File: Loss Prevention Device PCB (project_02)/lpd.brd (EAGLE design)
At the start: 48.3 x 58.4 mm, 4 parts, among them U2 GT-U7, U3 HM-10

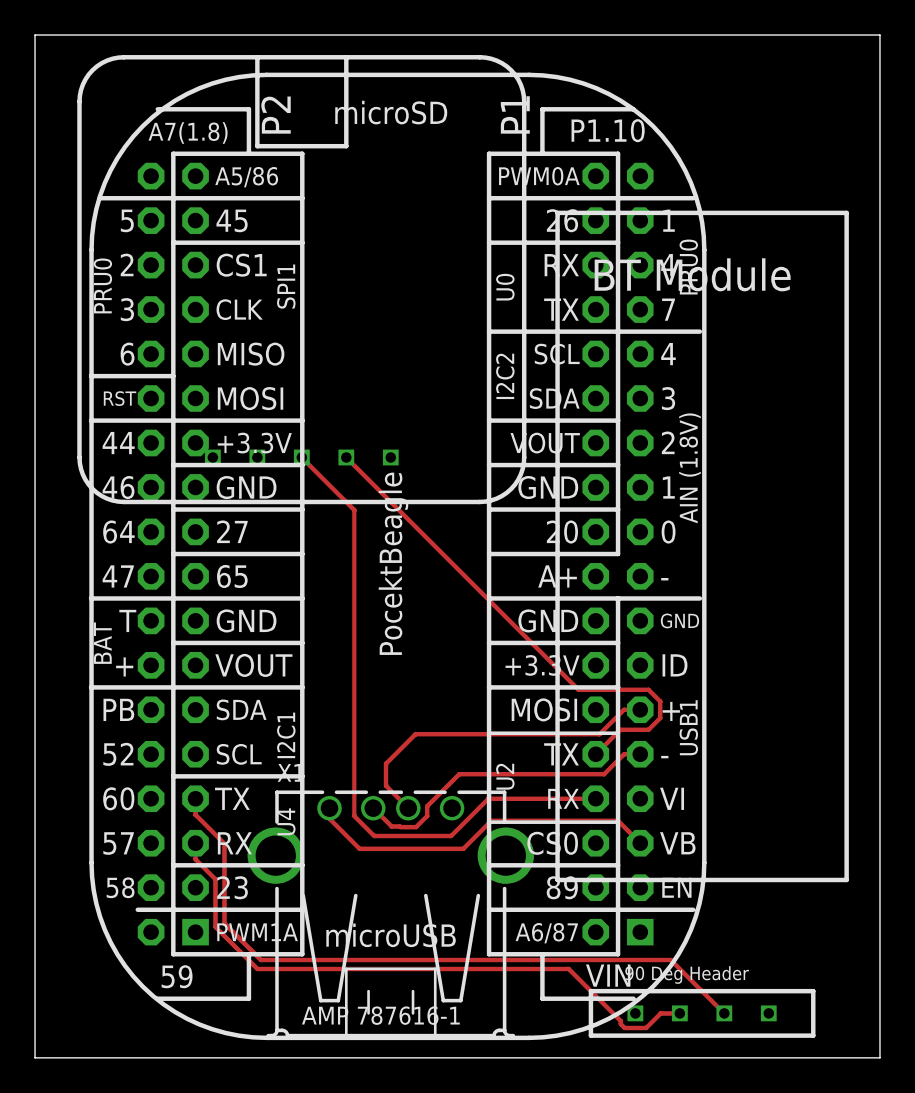
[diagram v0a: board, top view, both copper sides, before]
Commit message: Silkscreen cleanup
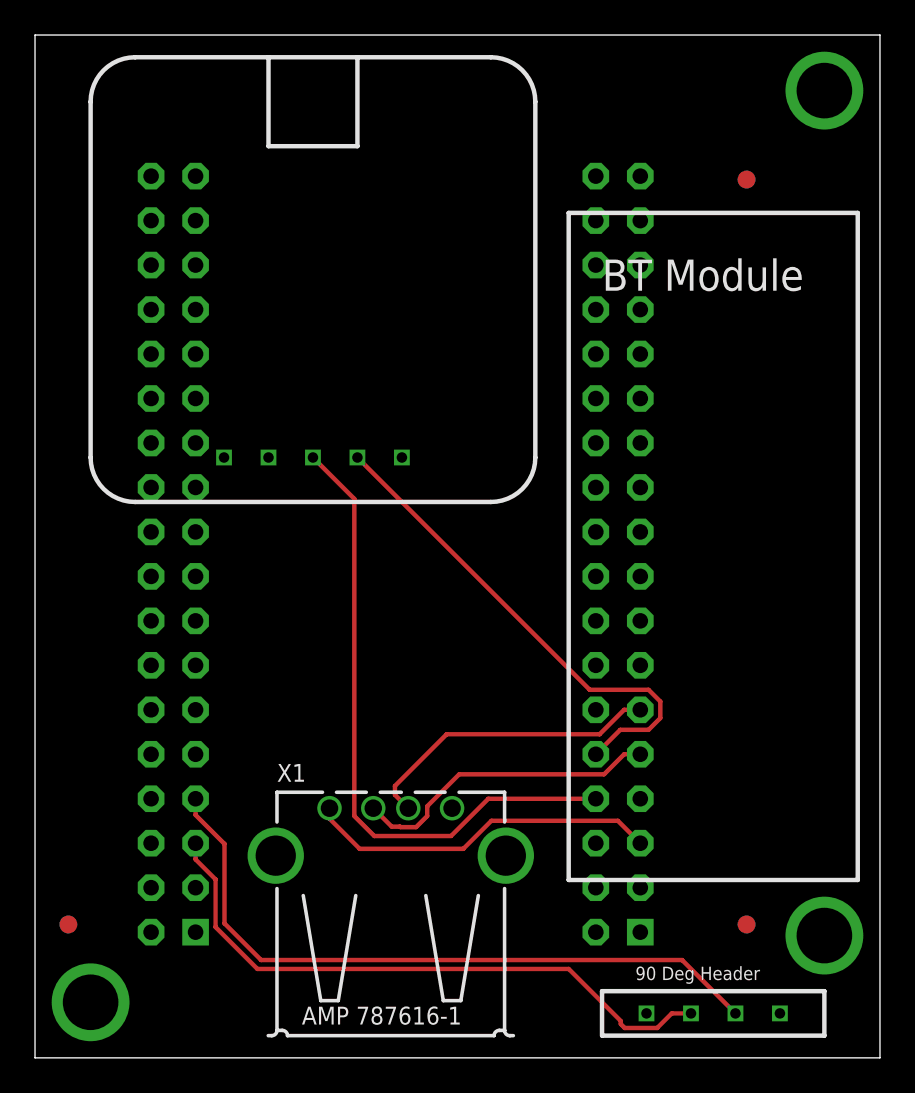
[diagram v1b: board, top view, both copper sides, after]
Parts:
- added FUD1, FUD2, FUD3, FUD4, FUD5, FUD6: FIDUCIAL, lpd:FIDUCIAL_40MIL
- added MGT1, MGT2, MGT3: MOUNTING_HOLE, lpd:MOUNTING_HOLE
- moved U2 0.63 mm to (3.17, 31.8)
- moved U3 0.63 mm to (32.4, 3.81)
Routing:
- net USB1.D+: track 18.9 -> 17.4 mm
- net UART4.TX: track 38.5 -> 39.1 mm
- net UART4.RX: track 34.6 -> 35.3 mm
- net UART2.TX: track 29.2 -> 28.6 mm
